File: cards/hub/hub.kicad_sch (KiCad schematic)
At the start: 28 parts, among them J1 BENCH 5V, J2 BUS, J3 BUS

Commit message: Hub: two 4 mm banana sockets for the bench supply (D058)
Bench supplies speak 4 mm banana: the leads plug in, polarity is the
colour, nothing is bare or screwed. The sockets stand on the hub's front
face (red +5V above black GND, 19.05 mm apart so a dual plug fits too)
because the card's edges are not reachable in the frame, 10 mm from the
next card and from the upright; edge-entry sockets, barrel jacks and XT
connectors all want a free edge. KiCad's Banana_Jack_1Pin footprint, a
6.1 mm plated hole for a panel-type socket (Cliff S16, Hirschmann BIL 20
or any red/black pair). The red socket's run to the 1.5 A polyfuse and
the black one's run up the left edge to the ground ring are pre-routed;
ERC 0, freerouting 2.4.1 in one pass, DRC 0 errors, 0 open, clean under
JLCPCB's minimum rules. Replaces the screw terminal of D057.

bom.py names the socket; order-1.md tables regenerated (pilot 320,
machine 7129); bring-up.md, cards/README.md, cards.md; DECISIONS D058.

Co-Authored-By: Claude Fable 5.1 <noreply@anthropic.com>
Claude-Session: https://claude.ai/code/session_01RktbhdQjDu7SpFpvkevyUU
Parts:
- removed J1: BENCH 5V, TerminalBlock_Phoenix:TerminalBlock_Phoenix_MKDS-1,5-2-5.08_1x02_P5.08mm_Horizontal, symbol Connector:Screw_Terminal_01x02
- removed J2: BUS, Connector_IDC:IDC-Header_2x32_P2.54mm_Vertical, symbol Connector_Generic:Conn_02x32_Odd_Even
- added J1: BENCH +5V, Connector:Banana_Jack_1Pin, symbol Connector_Generic:Conn_01x01
- added J2: BENCH GND, Connector:Banana_Jack_1Pin, symbol Connector_Generic:Conn_01x01
- added J4: BUS, Connector_IDC:IDC-Header_2x32_P2.54mm_Vertical, symbol Connector_Generic:Conn_02x32_Odd_Even
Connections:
- net +5V: now also J4.1 (Pin_1), J4.2 (Pin_2), J4.63 (Pin_63)
- net A0: now also J4.13 (Pin_13)
- net A1: now also J4.14 (Pin_14)
- net A2: now also J4.15 (Pin_15)
- net A3: now also J4.16 (Pin_16)
- net AB: now also J4.46 (Pin_46)
- net AI: now also J4.41 (Pin_41)
- net AO: now also J4.42 (Pin_42)
- net B0: now also J4.17 (Pin_17)
- net B1: now also J4.18 (Pin_18)
- net B2: now also J4.19 (Pin_19)
- net B3: now also J4.20 (Pin_20)
- net BA: now also J4.45 (Pin_45)
- net BI: now also J4.43 (Pin_43)
- net BO: now also J4.44 (Pin_44)
- net BUS0#: now also J4.9 (Pin_9)
- net BUS1#: now also J4.10 (Pin_10)
- net BUS2#: now also J4.11 (Pin_11)
- net BUS3#: now also J4.12 (Pin_12)
- net CF: now also J4.37 (Pin_37)
- net CLK: now also J4.5 (Pin_5)
- net EO: now also J4.40 (Pin_40)
- net F0: now also J4.60 (Pin_60)
- net F1: now also J4.61 (Pin_61)
- net FI: now also J4.52 (Pin_52)
- net GND: now also J2.1 (Pin_1), J4.3 (Pin_3), J4.4 (Pin_4), J4.6 (Pin_6), J4.64 (Pin_64), J4.8 (Pin_8)
- net HLT: now also J4.53 (Pin_53)
- net II: now also J4.49 (Pin_49)
- net INP: now also J4.62 (Pin_62)
- net IO: now also J4.48 (Pin_48)
- net M0: now also J4.29 (Pin_29)
- net M1: now also J4.30 (Pin_30)
- net M2: now also J4.31 (Pin_31)
- net M3: now also J4.32 (Pin_32)
- net M4: now also J4.33 (Pin_33)
- net M5: now also J4.34 (Pin_34)
- net M6: now also J4.35 (Pin_35)
- net M7: now also J4.36 (Pin_36)
- net MAI: now also J4.54 (Pin_54)
- net MI: now also J4.55 (Pin_55)
- net MO: now also J4.56 (Pin_56)
- net OI: now also J4.47 (Pin_47)
- net ONE: now also J4.59 (Pin_59)
- net PC0: now also J4.21 (Pin_21)
- net PC1: now also J4.22 (Pin_22)
- net PC2: now also J4.23 (Pin_23)
- net PC3: now also J4.24 (Pin_24)
- net PC4: now also J4.25 (Pin_25)
- net PC5: now also J4.26 (Pin_26)
- net PC6: now also J4.27 (Pin_27)
- net PC7: now also J4.28 (Pin_28)
- net PCE: now also J4.50 (Pin_50)
- net PCL: now also J4.51 (Pin_51)
- net RST: now also J4.7 (Pin_7)
- net SUB: now also J4.39 (Pin_39)
- net VBUS: now also J1.1 (Pin_1)
- net WRH: now also J4.58 (Pin_58)
- net WRL: now also J4.57 (Pin_57)
- net ZF: now also J4.38 (Pin_38)
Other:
- note added: "No logic on this card. Two 64-pin headers wired pin for pin: the top one takes one column face's ribbon, the bottom one the other's (docs/cards.md, D043). Power: 5 V from the bench supply, its banana leads into the two 4 mm sockets (D058; no USB, D057), through a 1.5 A polyfuse (D052: the machine draws up to about 1.2 A with every LED lit). The BUS0#..BUS3# pull-ups (10k) live here and nowhere el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"
- note removed: "No logic on this card. Two 64-pin headers wired pin for pin: the top one takes one column face's ribbon, the bottom one the other's (docs/cards.md, D043). Power: 5 V from the bench supply on the screw terminal, through a 1.5 A polyfuse (D052, D057: no USB, the machine draws up to about 1.2 A with every LED lit). The BUS0#..BUS3# pull-ups (10k) live here and nowhere else. The M0..M7 pull-downs (22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"

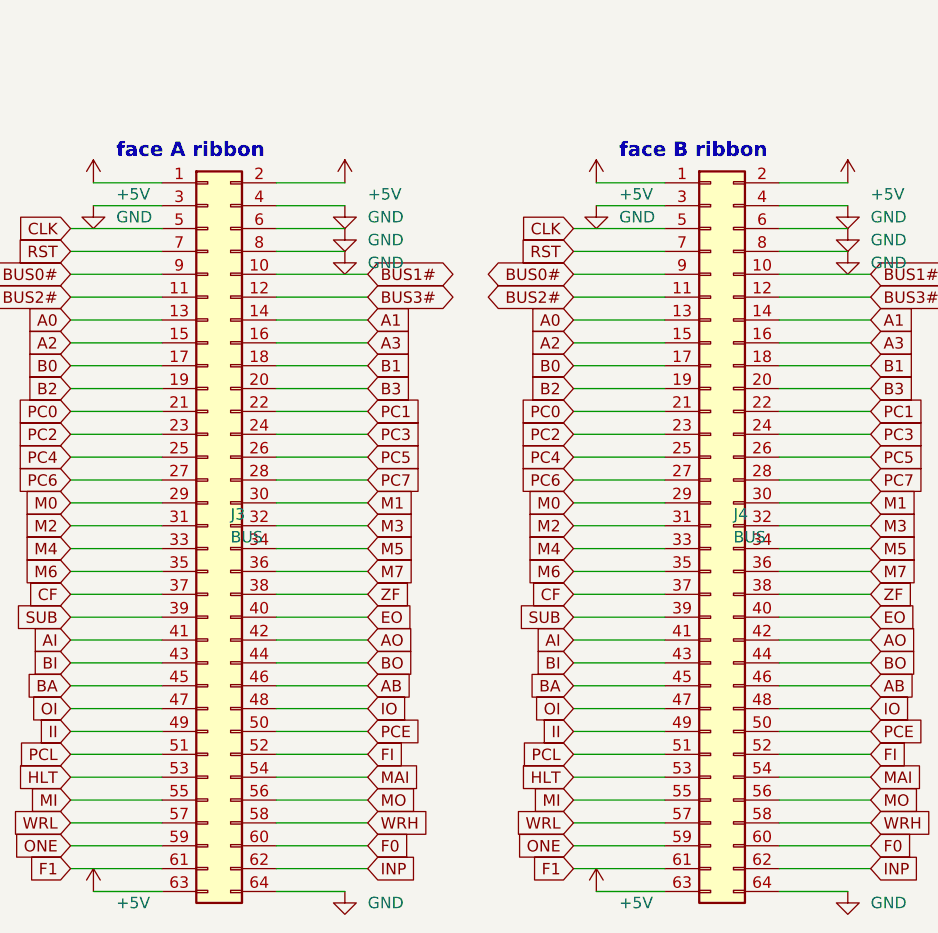
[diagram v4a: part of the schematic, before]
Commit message: The bus headers go on the back of all 26 boards, no track moved; the silkscreen refitted (D059, D062)
An IDC socket lies across its ribbon, so the ribbon could never run along a
row of cards as drawn. It runs behind them, and the 64-pin headers are
soldered on the back. This commit is that move, made in place on the routed
boards: no board was routed again.

How the header sits (D062): in the holes it had, turned over top to bottom,
notch toward the top edge. A pin of the odd row is then in the hole its even
neighbour had, so the two signals of every pair of pins change places: CLK
is pin 6, RST pin 8, +5V pins 1, 2 and 64. bus.py keeps both tables: PINS,
what the header's pins carry, and HOLES, what the copper was routed to.

The proof, on all 26 boards against 992a90f (sim/board_diff.py):
  netlist the same, element for element; every track, every via and every
  hole the same; each copper and mask layer differs by two pad shapes per
  header (pin 1's square went to the hole beside it, both on +5V) and the
  ground pour's outline round those two pads, nowhere else by more than a
  tenth of a micrometre.
sim/rebuild_check.py runs every builder into a scratch directory: each
writes the plan and the netlist that are committed, so a rebuild gives
this board. order_check.py --machine holds every pad of the 27 headers to
bus.py and requires them on the back.

What the move costs: on the ribbon RST had a ground conductor on both
sides; now one neighbour is BUS1#. tb_rst_neighbour.py puts the two lines
on the bench with every gate the routed boards hang on them: RST rises
0.28 to 0.43 V when BUS1# is released, against a lowest threshold of 0.8 V
(sim/results/rst_neighbour.md). The machine deck's crosstalk option now
couples the pins that are neighbours on the ribbon; the crosstalk stage of
the machine gate has to be run again on that order.

Silkscreen (pcb.fit_silk): every label to 1.0 mm where it has room, off
pads, vias, outlines and other labels, out from under the pa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
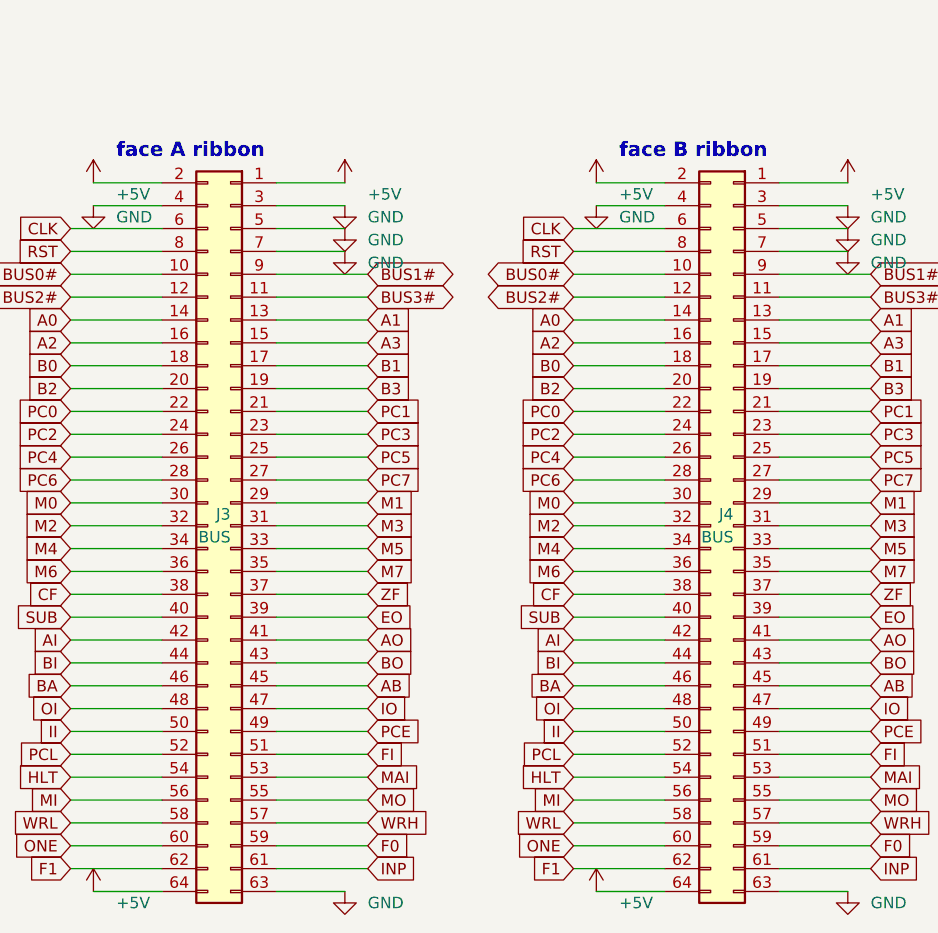
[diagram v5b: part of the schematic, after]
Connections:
- net +5V: now also J3.64 (Pin_64), J4.64 (Pin_64); no longer J3.63 (Pin_63), J4.63 (Pin_63)
- net A0: now also J3.14 (Pin_14), J4.14 (Pin_14); no longer J3.13 (Pin_13), J4.13 (Pin_13)
- net A1: now also J3.13 (Pin_13), J4.13 (Pin_13); no longer J3.14 (Pin_14), J4.14 (Pin_14)
- net A2: now also J3.16 (Pin_16), J4.16 (Pin_16); no longer J3.15 (Pin_15), J4.15 (Pin_15)
- net A3: now also J3.15 (Pin_15), J4.15 (Pin_15); no longer J3.16 (Pin_16), J4.16 (Pin_16)
- net AB: now also J3.45 (Pin_45), J4.45 (Pin_45); no longer J3.46 (Pin_46), J4.46 (Pin_46)
- net AI: now also J3.42 (Pin_42), J4.42 (Pin_42); no longer J3.41 (Pin_41), J4.41 (Pin_41)
- net AO: now also J3.41 (Pin_41), J4.41 (Pin_41); no longer J3.42 (Pin_42), J4.42 (Pin_42)
- net B0: now also J3.18 (Pin_18), J4.18 (Pin_18); no longer J3.17 (Pin_17), J4.17 (Pin_17)
- net B1: now also J3.17 (Pin_17), J4.17 (Pin_17); no longer J3.18 (Pin_18), J4.18 (Pin_18)
- net B2: now also J3.20 (Pin_20), J4.20 (Pin_20); no longer J3.19 (Pin_19), J4.19 (Pin_19)
- net B3: now also J3.19 (Pin_19), J4.19 (Pin_19); no longer J3.20 (Pin_20), J4.20 (Pin_20)
- net BA: now also J3.46 (Pin_46), J4.46 (Pin_46); no longer J3.45 (Pin_45), J4.45 (Pin_45)
- net BI: now also J3.44 (Pin_44), J4.44 (Pin_44); no longer J3.43 (Pin_43), J4.43 (Pin_43)
- net BO: now also J3.43 (Pin_43), J4.43 (Pin_43); no longer J3.44 (Pin_44), J4.44 (Pin_44)
- net BUS0#: now also J3.10 (Pin_10), J4.10 (Pin_10); no longer J3.9 (Pin_9), J4.9 (Pin_9)
- net BUS1#: now also J3.9 (Pin_9), J4.9 (Pin_9); no longer J3.10 (Pin_10), J4.10 (Pin_10)
- net BUS2#: now also J3.12 (Pin_12), J4.12 (Pin_12); no longer J3.11 (Pin_11), J4.11 (Pin_11)
- net BUS3#: now also J3.11 (Pin_11), J4.11 (Pin_11); no longer J3.12 (Pin_12), J4.12 (Pin_12)
- net CF: now also J3.38 (Pin_38), J4.38 (Pin_38); no longer J3.37 (Pin_37), J4.37 (Pin_37)
- net CLK: now also J3.6 (Pin_6), J4.6 (Pin_6); no longer J3.5 (Pin_5), J4.5 (Pin_5)
- net EO: now also J3.39 (Pin_39), J4.39 (Pin_39); no longer J3.40 (Pin_40), J4.40 (Pin_40)
- net F0: now also J3.59 (Pin_59), J4.59 (Pin_59); no longer J3.60 (Pin_60), J4.60 (Pin_60)
- net F1: now also J3.62 (Pin_62), J4.62 (Pin_62); no longer J3.61 (Pin_61), J4.61 (Pin_61)
- net FI: now also J3.51 (Pin_51), J4.51 (Pin_51); no longer J3.52 (Pin_52), J4.52 (Pin_52)
- net GND: now also J3.5 (Pin_5), J3.63 (Pin_63), J3.7 (Pin_7), J4.5 (Pin_5), J4.63 (Pin_63), J4.7 (Pin_7); no longer J3.6 (Pin_6), J3.64 (Pin_64), J3.8 (Pin_8), J4.6 (Pin_6), J4.64 (Pin_64), J4.8 (Pin_8)
- net HLT: now also J3.54 (Pin_54), J4.54 (Pin_54); no longer J3.53 (Pin_53), J4.53 (Pin_53)
- net II: now also J3.50 (Pin_50), J4.50 (Pin_50); no longer J3.49 (Pin_49), J4.49 (Pin_49)
- net INP: now also J3.61 (Pin_61), J4.61 (Pin_61); no longer J3.62 (Pin_62), J4.62 (Pin_62)
- net IO: now also J3.47 (Pin_47), J4.47 (Pin_47); no longer J3.48 (Pin_48), J4.48 (Pin_48)
- net M0: now also J3.30 (Pin_30), J4.30 (Pin_30); no longer J3.29 (Pin_29), J4.29 (Pin_29)
- net M1: now also J3.29 (Pin_29), J4.29 (Pin_29); no longer J3.30 (Pin_30), J4.30 (Pin_30)
- net M2: now also J3.32 (Pin_32), J4.32 (Pin_32); no longer J3.31 (Pin_31), J4.31 (Pin_31)
- net M3: now also J3.31 (Pin_31), J4.31 (Pin_31); no longer J3.32 (Pin_32), J4.32 (Pin_32)
- net M4: now also J3.34 (Pin_34), J4.34 (Pin_34); no longer J3.33 (Pin_33), J4.33 (Pin_33)
- net M5: now also J3.33 (Pin_33), J4.33 (Pin_33); no longer J3.34 (Pin_34), J4.34 (Pin_34)
- net M6: now also J3.36 (Pin_36), J4.36 (Pin_36); no longer J3.35 (Pin_35), J4.35 (Pin_35)
- net M7: now also J3.35 (Pin_35), J4.35 (Pin_35); no longer J3.36 (Pin_36), J4.36 (Pin_36)
- net MAI: now also J3.53 (Pin_53), J4.53 (Pin_53); no longer J3.54 (Pin_54), J4.54 (Pin_54)
- net MI: now also J3.56 (Pin_56), J4.56 (Pin_56); no longer J3.55 (Pin_55), J4.55 (Pin_55)
- net MO: now also J3.55 (Pin_55), J4.55 (Pin_55); no longer J3.56 (Pin_56), J4.56 (Pin_56)
- net OI: now also J3.48 (Pin_48), J4.48 (Pin_48); no longer J3.47 (Pin_47), J4.47 (Pin_47)
- net ONE: now also J3.60 (Pin_60), J4.60 (Pin_60); no longer J3.59 (Pin_59), J4.59 (Pin_59)
- net PC0: now also J3.22 (Pin_22), J4.22 (Pin_22); no longer J3.21 (Pin_21), J4.21 (Pin_21)
- net PC1: now also J3.21 (Pin_21), J4.21 (Pin_21); no longer J3.22 (Pin_22), J4.22 (Pin_22)
- net PC2: now also J3.24 (Pin_24), J4.24 (Pin_24); no longer J3.23 (Pin_23), J4.23 (Pin_23)
- net PC3: now also J3.23 (Pin_23), J4.23 (Pin_23); no longer J3.24 (Pin_24), J4.24 (Pin_24)
- net PC4: now also J3.26 (Pin_26), J4.26 (Pin_26); no longer J3.25 (Pin_25), J4.25 (Pin_25)
- net PC5: now also J3.25 (Pin_25), J4.25 (Pin_25); no longer J3.26 (Pin_26), J4.26 (Pin_26)
- net PC6: now also J3.28 (Pin_28), J4.28 (Pin_28); no longer J3.27 (Pin_27), J4.27 (Pin_27)
- net PC7: now also J3.27 (Pin_27), J4.27 (Pin_27); no longer J3.28 (Pin_28), J4.28 (Pin_28)
- net PCE: now also J3.49 (Pin_49), J4.49 (Pin_49); no longer J3.50 (Pin_50), J4.50 (Pin_50)
- net PCL: now also J3.52 (Pin_52), J4.52 (Pin_52); no longer J3.51 (Pin_51), J4.51 (Pin_51)
- net RST: now also J3.8 (Pin_8), J4.8 (Pin_8); no longer J3.7 (Pin_7), J4.7 (Pin_7)
- net SUB: now also J3.40 (Pin_40), J4.40 (Pin_40); no longer J3.39 (Pin_39), J4.39 (Pin_39)
- net WRH: now also J3.57 (Pin_57), J4.57 (Pin_57); no longer J3.58 (Pin_58), J4.58 (Pin_58)
- net WRL: now also J3.58 (Pin_58), J4.58 (Pin_58); no longer J3.57 (Pin_57), J4.57 (Pin_57)
- net ZF: now also J3.37 (Pin_37), J4.37 (Pin_37); no longer J3.38 (Pin_38), J4.38 (Pin_38)
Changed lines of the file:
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@@
 	(symbol
 		(lib_id "Connector_Generic:Conn_02x32_Odd_Even")
-		(at 76.2 177.8 0)
+		(at 78.74 177.8 0)
+		(mirror y)
 		(unit 1)
 		(body_style 1)
@@
 	(symbol
 		(lib_id "Connector_Generic:Conn_02x32_Odd_Even")
-		(at 132.08 177.8 0)
+		(at 134.62 177.8 0)
+		(mirror y)
 		(unit 1)
 		(body_style 1)

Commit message: Hub: sockets that are soldered in, and the crowbar (D061, D063)
The hub was on hold for two reasons, and gets the protection that was
decided while it waited.

Sockets. The panel sockets of D058 put a bushing, a nut and a solder tag
15 mm behind the board, where the frame's rail is. The new ones are Cal Test
CT3151V1 (red -2, black -0): they stand on the board on four solder pins
with 1.6 mm behind it. The footprint is drawn from the maker's drawing
(P315100 rev H, sheet 3: four 1.60 mm holes on a 4.76 mm diamond, body
13.5 mm) and lives in lib/nibble.pretty; KiCad's own CT3151 footprint is the
one that lies on its side. The keep-outs and the hand-led CLK and RST of
the nut's time are gone.

Crowbar, five parts behind the polyfuse: 1N4735A (6.2 V) into the gate of a
BT151-500R across the rail, 100 ohm and 100 nF on the gate, a 1N5408 across
the rail the other way round. The values are the bench's
(sim/results/crowbar.md). The loop that carries the supply's limit once it
has fired (socket, fuse, SCR, socket) is 2 mm copper. The SCR's tab faces the
fuse, with room above it for a clip-on heatsink.

The first placement had the gate's three parts behind the cathode's track
and the router left one net open in three attempts; on the gate pin's side
it routes in one. The crowbar's parts are created last, so every part that
is in the machine's simulation keeps its reference: the hub's SPICE export
is the same line for line.

The gate's pins rule knows the three new parts (an SCR across the rail with
its gate on neither; a zener and a diode that stand against the rail on
purpose) and is tested on eight more made-up faults. On the hub as built:
every check passes but `clean`, which is this commit.

Co-Authored-By: Claude Fable 5.1 <noreply@anthropic.com>
Claude-Session: https://claude.ai/code/session_01RktbhdQjDu7SpFpvkevyUU
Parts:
- added C3: 100n, Capacitor_THT:C_Disc_D5.0mm_W2.5mm_P2.50mm, symbol Device:C
- added D2: 1N4735A, Diode_THT:D_DO-41_SOD81_P10.16mm_Horizontal, symbol Device:D_Zener
- added D3: 1N5408, Diode_THT:D_DO-201AD_P15.24mm_Horizontal, symbol Device:D
- added Q1: BT151-500R, Package_TO_SOT_THT:TO-220-3_Vertical, symbol Device:Q_SCR_KAG
- added R14: 100, Resistor_THT:R_Axial_DIN0207_L6.3mm_D2.5mm_P5.08mm_Vertical, symbol Device:R
- J1, J2: footprint Connector:Banana_Jack_1Pin -> nibble:Banana_CalTest_CT3151V1_Vertical
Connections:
- net +5V: now also D2.1 (K), D3.1 (K), Q1.2 (A)
- net GND: now also C3.2, D3.2 (A), Q1.1 (K), R14.2
- new net: C3.1, D2.2 (A), Q1.3 (G), R14.1
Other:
- note added: "CROWBAR (D061): above about 6.3 to 7.8 V the zener fires the SCR, which holds the rail near 1 V until the supply is switched off; the diode takes crossed leads. Run the supply with its limit at 1.5 A: the SCR then holds a fault for as long as it takes to notice. At 3 A or more it wants a clip-on heatsink."
